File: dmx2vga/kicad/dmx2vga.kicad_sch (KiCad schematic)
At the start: 14 parts, among them J1 DMX In, J2 DMX Thru, J3 Programming Pins, J4 DE15_Receptacle_HighDensity, SW1 RotaryEncoder_Switch, SW2 SW_Push, U1 Olimex_MOD-WIFI-ESP8266-DEV, U2 MAX485E

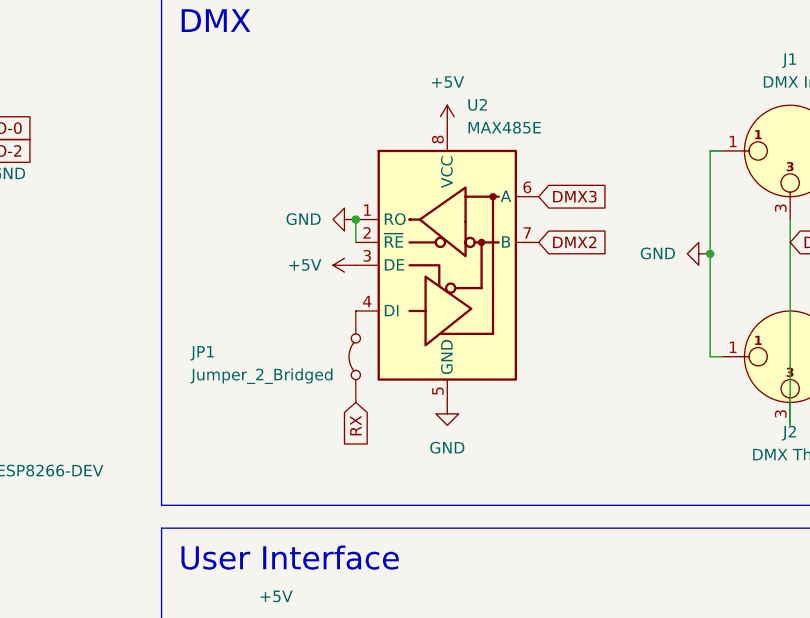
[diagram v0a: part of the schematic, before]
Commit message: feat(kicad): fix max485 connections
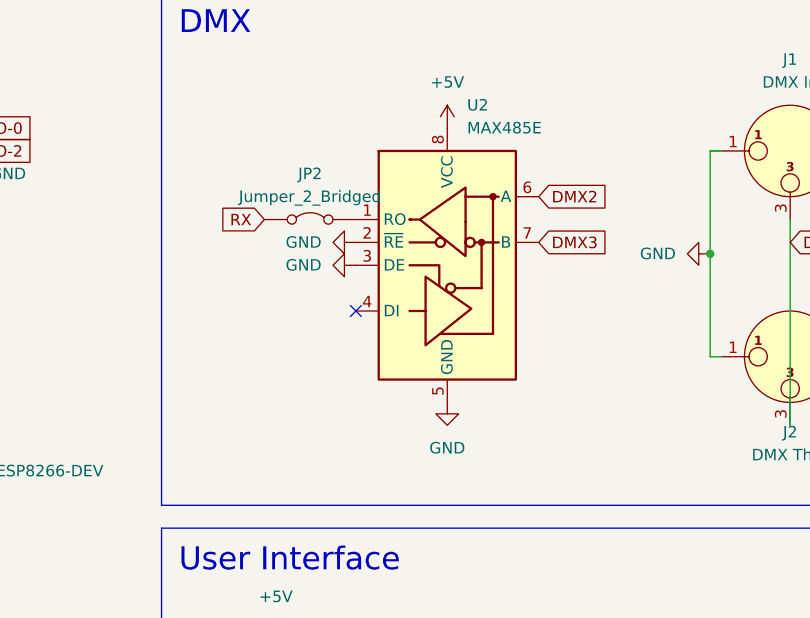
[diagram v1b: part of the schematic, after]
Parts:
- removed JP1: Jumper_2_Bridged, Connector_PinSocket_2.54mm:PinSocket_1x02_P2.54mm_Vertical, symbol Jumper:Jumper_2_Bridged
- added JP2: Jumper_2_Bridged, symbol Jumper:Jumper_2_Bridged
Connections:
- net +5V: no longer U2.3 (DE)
- net DMX2: now also U2.6 (A); no longer U2.7 (B)
- net DMX3: now also U2.7 (B); no longer U2.6 (A)
- net GND: now also U2.3 (DE); no longer U2.1 (RO)
- net RX: now also JP2.1 (A)
- new net: JP2.2 (B), U2.1 (RO)
- no-connect marks 10 -> 11
